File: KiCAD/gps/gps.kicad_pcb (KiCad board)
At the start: 2 copper layers, 87 x 119 mm, 57 parts, among them J1 Conn_01x04_Socket, J2 Conn_02x06_Odd_Even, J4 Conn_02x04_Odd_Even, J5 Conn_02x20_Odd_Even, J6 Conn_01x02_Pin, J7 PJ-037A, J8 1758050, J9 CU01SAH0S00, Q1 SQJ746ELP-T1_GE3, Q2 SQJ746ELP-T1_GE3, Q3 IRLML6344TRPBF, U1 AP74502QTA8-7, U2 AP22654WU-7, U3 AP74502QTA8-7

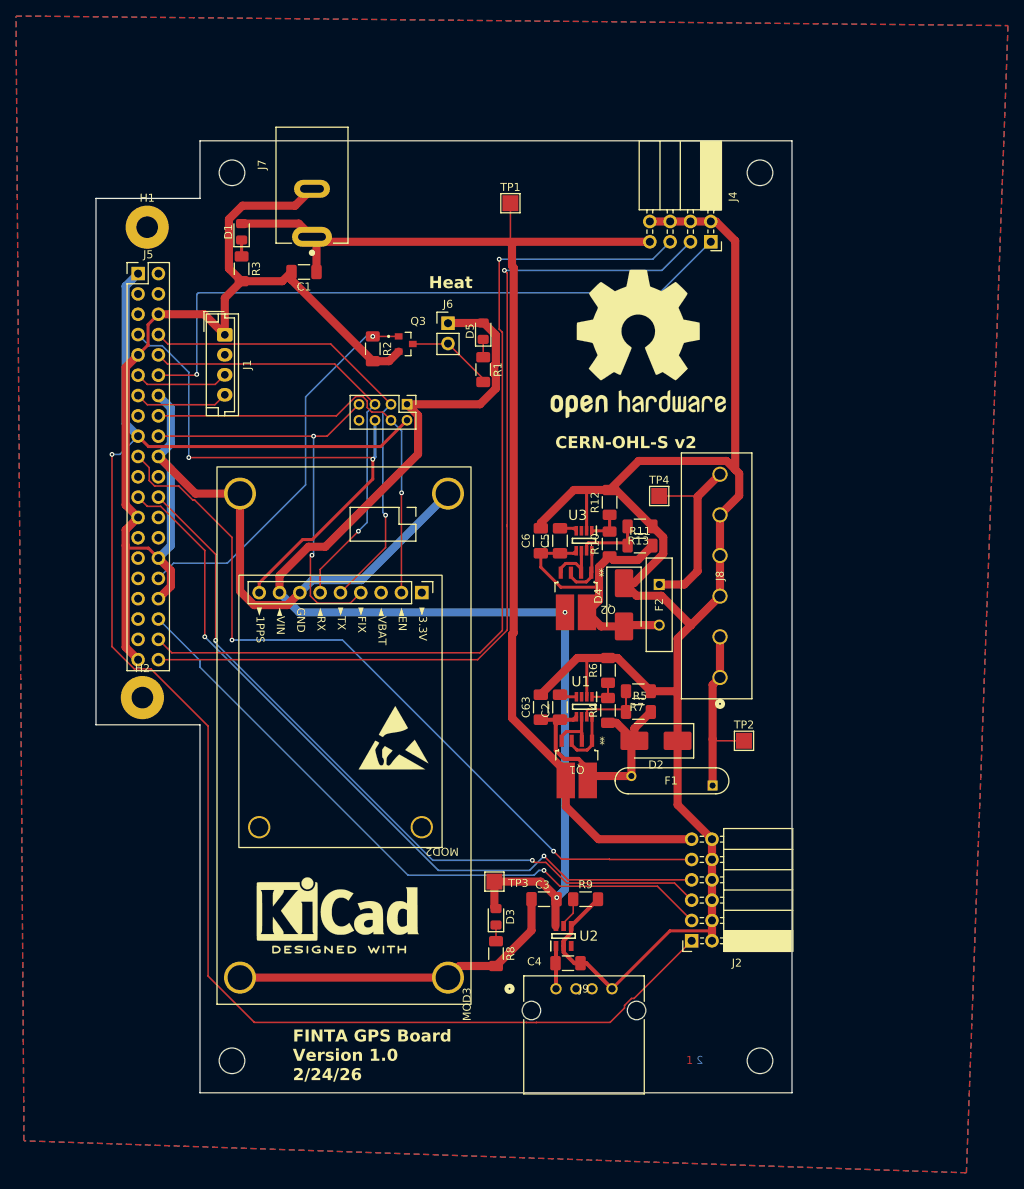
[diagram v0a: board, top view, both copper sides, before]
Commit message: Added FPGA debug header and debug LEDs
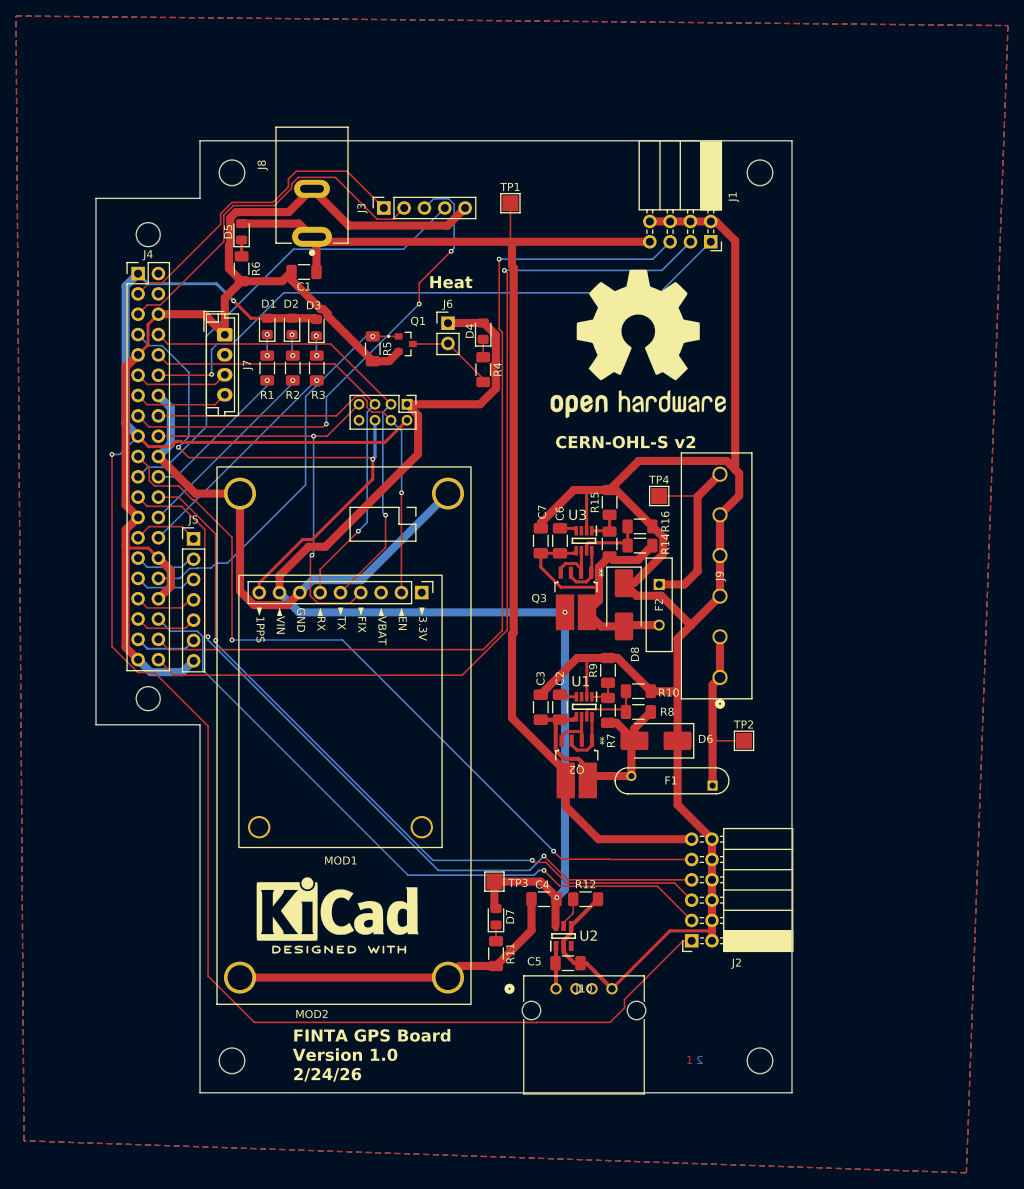
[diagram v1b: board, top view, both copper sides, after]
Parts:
- removed the REF** at (84.2, 109.6)
- added D1: LED, LED_SMD:LED_0805_2012Metric_Pad1.15x1.40mm_HandSolder, F.Cu at (68.4, 58.2)
- added D2: LED, LED_SMD:LED_0805_2012Metric_Pad1.15x1.40mm_HandSolder, F.Cu at (71.5, 58.2)
- added D3: LED, LED_SMD:LED_0805_2012Metric_Pad1.15x1.40mm_HandSolder, F.Cu at (74.5, 58.4)
- added J3: Conn_01x05_Pin, Connector_PinSocket_2.54mm:PinSocket_1x05_P2.54mm_Vertical, F.Cu at (83.0, 43.4)
- added J5: Conn_01x07_Pin, Connector_PinHeader_2.54mm:PinHeader_1x07_P2.54mm_Vertical, F.Cu at (59.2, 84.8)
- added R1: 240, Resistor_SMD:R_1206_3216Metric_Pad1.30x1.75mm_HandSolder, F.Cu at (68.4, 63.4)
- added R2: 240, Resistor_SMD:R_1206_3216Metric_Pad1.30x1.75mm_HandSolder, F.Cu at (71.6, 63.4)
- added R3: 240, Resistor_SMD:R_1206_3216Metric_Pad1.30x1.75mm_HandSolder, F.Cu at (74.6, 63.4)
- H1, H2: value MountingHole_Pad -> MountingHole; footprint MountingHole:MountingHole_2.7mm_M2.5_Pad -> MountingHole:MountingHole_3mm
- moved H1 0.94 mm to (53.5, 46.7)
- moved H2 0.74 mm to (53.5, 104.7)
- renumbered C63 to C3, C3 to C4, C4 to C5, C5 to C6, C6 to C7, D5 to D4, D1 to D5, D2 to D6, D3 to D7, D4 to D8, J4 to J1, J9 to J10, J5 to J4, J1 to J7, J7 to J8, J8 to J9, MOD2 to MOD1, MOD3 to MOD2, Q3 to Q1, Q1 to Q2, Q2 to Q3, R7 to R10, R8 to R11, R9 to R12, R10 to R13, R11 to R14, R12 to R15, R13 to R16, R1 to R4, R2 to R5, R3 to R6, R4 to R7, R5 to R8, R6 to R9
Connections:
- J4 pad 15: unconnected-(J5-Pin_15-Pad15) -> Net-(J3-Pin_3)
- J4 pad 21: unconnected-(J5-Pin_21-Pad21) -> Net-(J3-Pin_4)
- J4 pad 22: unconnected-(J5-Pin_22-Pad22) -> Net-(J4-Pin_22)
- J4 pad 26: unconnected-(J5-Pin_26-Pad26) -> Net-(J4-Pin_26)
- J4 pad 27: unconnected-(J5-Pin_27-Pad27) -> Net-(J4-Pin_27)
- J4 pad 28: unconnected-(J5-Pin_28-Pad28) -> Net-(J4-Pin_28)
- J4 pad 29: unconnected-(J5-Pin_29-Pad29) -> Net-(J4-Pin_29)
- J4 pad 3: unconnected-(J5-Pin_3-Pad3) -> Net-(J3-Pin_1)
- J4 pad 31: unconnected-(J5-Pin_31-Pad31) -> Net-(J4-Pin_31)
- J4 pad 33: unconnected-(J5-Pin_33-Pad33) -> Net-(J4-Pin_33)
- J4 pad 35: unconnected-(J5-Pin_35-Pad35) -> Net-(J4-Pin_35)
- J4 pad 37: unconnected-(J5-Pin_37-Pad37) -> Net-(J4-Pin_37)
- J4 pad 5: unconnected-(J5-Pin_5-Pad5) -> Net-(J3-Pin_2)
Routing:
- net Net-(J3-Pin_3): track 0.00 -> 62.8 mm, vias 0 -> 3
- net Net-(J3-Pin_4): track 0.00 -> 58.9 mm
- net Net-(J3-Pin_2): track 0.00 -> 45.3 mm
- net Net-(J3-Pin_1): track 0.00 -> 40.3 mm
- net Net-(J4-Pin_28): track 0.00 -> 27.9 mm, vias 0 -> 1
- net +3V3: track 200.0 -> 225.2 mm, vias 1 -> 2
- net Net-(J4-Pin_26): track 0.00 -> 24.1 mm, vias 0 -> 1
- net Net-(J4-Pin_22): track 0.00 -> 19.0 mm, vias 0 -> 1
- net GND: track 467.4 -> 483.7 mm
- net Net-(J4-Pin_37): track 0.00 -> 7.86 mm
- net Net-(J4-Pin_27): track 0.00 -> 7.84 mm
- net Net-(J4-Pin_35): track 0.00 -> 7.84 mm
- net Net-(J4-Pin_33): track 0.00 -> 7.74 mm
- net Net-(J4-Pin_29): track 0.00 -> 7.74 mm
- net Net-(J4-Pin_31): track 0.00 -> 7.74 mm
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
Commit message: gps PCB 1.1
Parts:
- removed J3: Conn_01x05_Pin, Connector_PinSocket_2.54mm:PinSocket_1x05_P2.54mm_Vertical
- added C10: 0.1uf, Capacitor_SMD:C_0603_1608Metric_Pad1.08x0.95mm_HandSolder, F.Cu at (79.9, 56.6)
- added C11: 0.1uf, Capacitor_SMD:C_1206_3216Metric_Pad1.33x1.80mm_HandSolder, F.Cu at (67.6, 86.6)
- added C35: 10uf, Capacitor_SMD:C_1206_3216Metric_Pad1.33x1.80mm_HandSolder, F.Cu at (79.0, 73.2)
- added C36: 10uf, Capacitor_SMD:C_1206_3216Metric_Pad1.33x1.80mm_HandSolder, F.Cu at (81.5, 73.2)
- added C38: 0.22uf C0G, Capacitor_SMD:C_0603_1608Metric_Pad1.08x0.95mm_HandSolder, F.Cu at (75.4, 80.5)
- added C39: 0.22uf, Capacitor_SMD:C_1206_3216Metric_Pad1.33x1.80mm_HandSolder, F.Cu at (72.9, 78.5)
- added C8: 0.1uf, Capacitor_SMD:C_0603_1608Metric_Pad1.08x0.95mm_HandSolder, F.Cu at (61.0, 67.1)
- added C9: 0.1uf, Capacitor_SMD:C_0603_1608Metric_Pad1.08x0.95mm_HandSolder, F.Cu at (61.0, 64.8)
- added R17: 4.7K, Resistor_SMD:R_1206_3216Metric_Pad1.30x1.75mm_HandSolder, F.Cu at (63.2, 51.6)
- added R18: 4.7K, Resistor_SMD:R_1206_3216Metric_Pad1.30x1.75mm_HandSolder, F.Cu at (65.8, 53.3)
- added R21: 1K 0.01% 5ppm, Resistor_SMD:R_0805_2012Metric_Pad1.20x1.40mm_HandSolder, F.Cu at (68.6, 78.0)
- added R22: 10K 0.01% 5ppm, Resistor_SMD:R_0805_2012Metric_Pad1.20x1.40mm_HandSolder, F.Cu at (70.6, 78.0)
- added R23: 100, Resistor_SMD:R_1206_3216Metric_Pad1.30x1.75mm_HandSolder, F.Cu at (65.0, 70.6)
- added U16: AMS1117-1.8, Package_TO_SOT_SMD:SOT-223-3_TabPin2, F.Cu at (81.3, 80.8)
- added U19: CDCE913PWR, ! Texas Instruments:SOP65P640X120-14N, F.Cu at (66.8, 65.3)
- added U4: TMP1075D, Package_SO:SO-8_3.9x4.9mm_P1.27mm, F.Cu at (74.4, 58.5)
- added U7: DAC8563SDGSR, ! Texas Instruments:SOP50P490X110-10N, F.Cu at (72.4, 84.1)
- added U9: OPA192IDBVR, ! Texas Instruments:SOT95P280X145-5N, F.Cu at (69.1, 73.2)
- added Y1: 7M-27.000MEEQ-T, ! TXC Corporation:XTAL_7M-27.000MEEQ-T, F.Cu at (66.8, 60.2)
- J5: value Conn_01x07_Pin -> Conn_01x05_Pin; footprint Connector_PinHeader_2.54mm:PinHeader_1x07_P2.54mm_Vertical -> Connector_PinHeader_2.54mm:PinHeader_1x05_P2.54mm_Vertical
- J7: footprint Connector_JST:JST_EH_B4B-EH-A_1x04_P2.50mm_Vertical -> Connector_JST:JST_PH_B4B-PH-K_1x04_P2.00mm_Vertical
- moved D3 92.5 mm to (81.5, 150.6), turned to 0 degrees
- moved D2 89.9 mm to (81.7, 147.5), turned to 0 degrees
- moved R3 87.2 mm to (76.5, 150.6), turned to 180 degrees
- moved D1 87.2 mm to (81.7, 144.4), turned to 0 degrees
- moved R2 84.4 mm to (76.5, 147.6), turned to 180 degrees
- moved R1 81.4 mm to (76.5, 144.4), turned to 180 degrees
- moved J4 48.3 mm to (54.8, 99.9), turned to 180 degrees
- moved J5 23.0 mm to (59.4, 61.7), turned to 180 degrees
- moved R6 22.9 mm to (85.9, 41.1), turned to 90 degrees
- moved D5 20.7 mm to (85.9, 45.7), turned to -90 degrees
- moved TP1 16.6 mm to (84.8, 51.8)
- moved J7 14.5 mm to (60.5, 45.0), turned to 0 degrees
- moved J8 4.49 mm to (78.5, 47.2)
- moved C1 3.73 mm to (76.7, 51.8)
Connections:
- J2 pad 3: 10MHZ Square -> 10MHz OCXO
- J4 pad 10: GPSRX -> unconnected-(J4-Pin_10-Pad10)
- J4 pad 11: SDA -> unconnected-(J4-Pin_11-Pad11)
- J4 pad 12: ~{SPI_IRIG_CS} -> unconnected-(J4-Pin_12-Pad12)
- J4 pad 13: SCL -> ~{SPI_OCXO_CS}
- J4 pad 15: Net-(J3-Pin_3) -> SPI_SCLK
- J4 pad 16: GPSRESET -> ~{SPI_VCXO_CS}
- J4 pad 18: TP2/FIX -> SPI_MOSI
- J4 pad 19: SPI_MOSI -> ~{SPI_IRIG_CS}
- J4 pad 21: Net-(J3-Pin_4) -> SPI_IRIG_SCLK
- J4 pad 22: Net-(J4-Pin_22) -> SPI_IRIG_MOSI
- J4 pad 23: SPI_SCLK -> GPSRESET
- J4 pad 24: ~{SPI_OCXO_CS} -> 10MHz OCXO
- J4 pad 26: Net-(J4-Pin_26) -> 1PPS
- J4 pad 27: Net-(J4-Pin_27) -> GPSRX
- J4 pad 28: Net-(J4-Pin_28) -> TP2/FIX
- J4 pad 29: Net-(J4-Pin_29) -> GPSTX
- J4 pad 3: Net-(J3-Pin_1) -> Net-(J4-Pin_3)
- J4 pad 36: 10MHZ Square -> 10MHz VCXO
- J4 pad 38: SPI_IRIG_MOSI -> SCL
- J4 pad 40: SPI_IRIG_SCLK -> SDA
- J4 pad 5: Net-(J3-Pin_2) -> Net-(J4-Pin_5)
- J4 pad 7: 1PPS -> Net-(J4-Pin_7)
- J4 pad 8: GPSTX -> unconnected-(J4-Pin_8-Pad8)
- J5 pad 1: Net-(J4-Pin_27) -> Net-(J4-Pin_31)
- J5 pad 2: Net-(J4-Pin_29) -> Net-(J4-Pin_33)
- J5 pad 3: Net-(J4-Pin_31) -> Net-(J4-Pin_35)
- J5 pad 4: Net-(J4-Pin_33) -> Net-(J4-Pin_37)
- J5 pad 5: Net-(J4-Pin_35) -> GND
- R1 pad 2: Net-(J4-Pin_22) -> Net-(J4-Pin_7)
- R2 pad 2: Net-(J4-Pin_26) -> Net-(J4-Pin_5)
- R3 pad 2: Net-(J4-Pin_28) -> Net-(J4-Pin_3)
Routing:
- net GND: track 483.7 -> 612.2 mm
- net 10MHz OCXO: track 0.00 -> 111.3 mm, vias 0 -> 1
- net 10MHZ Square: track 85.2 -> 0.00 mm, vias 1 -> 0
- net Net-(J4-Pin_7): track 0.00 -> 65.4 mm
- net Net-(J4-Pin_5): track 0.00 -> 64.5 mm
- net Net-(J4-Pin_3): track 0.00 -> 63.5 mm
- net Net-(J3-Pin_3): track 62.8 -> 0.00 mm, vias 3 -> 0
- net Net-(J3-Pin_4): track 58.9 -> 0.00 mm
- net Net-(J3-Pin_2): track 45.3 -> 0.00 mm
- net SCL: track 11.8 -> 54.1 mm, vias 0 -> 2
- net Net-(J3-Pin_1): track 40.3 -> 0.00 mm
- net +3V3: track 225.2 -> 260.6 mm, vias 2 -> 3
- net TP2/FIX: track 54.1 -> 87.4 mm
- net +1V8: track 0.00 -> 33.3 mm
- net SDA: track 11.8 -> 44.6 mm, vias 0 -> 2
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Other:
- board text added: "FINTA GPS Board Version 1.1 3/24/26"
- board text removed: "FINTA GPS Board Version 1.0 2/24/26"
